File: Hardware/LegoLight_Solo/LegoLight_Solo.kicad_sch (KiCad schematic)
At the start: 37 parts, among them IC1 PAM2401SCADJ, J1 USB4105-GF-A, J2 103P012BB100, J3 103P012BB100, J4 Conn_01x02_Socket, J5 VEML7700-TT, J8 I2C, U1 MCP73831-2-OT, U2 KXTJ3-1057

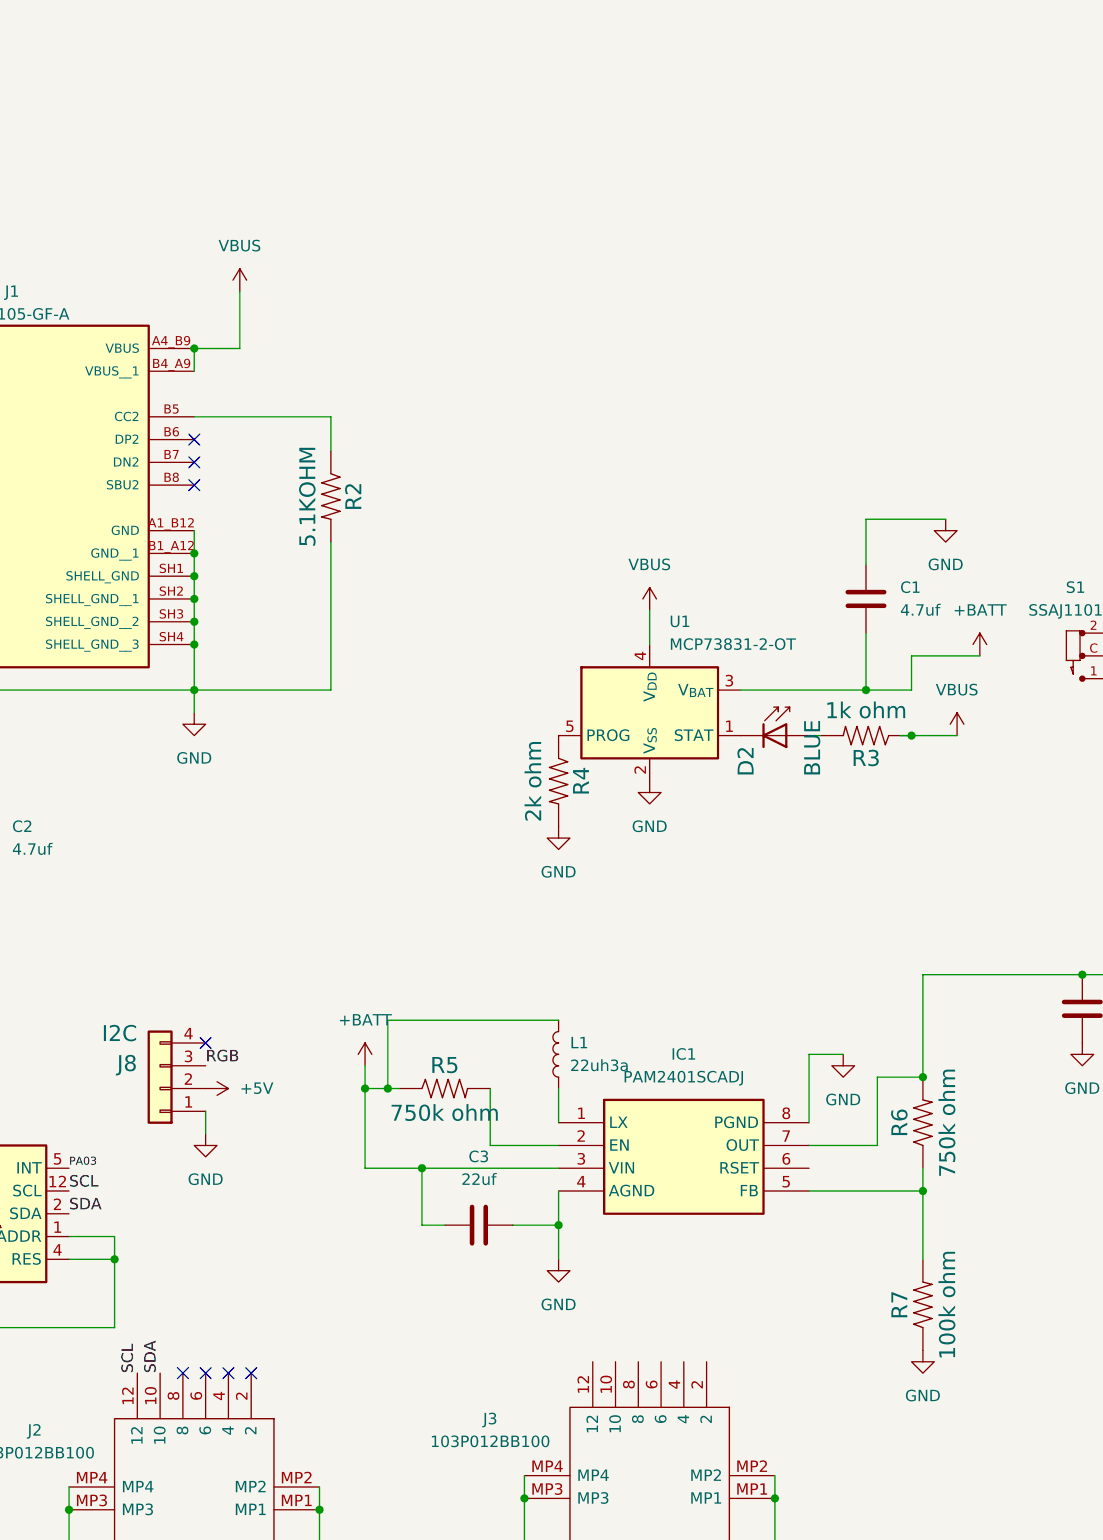
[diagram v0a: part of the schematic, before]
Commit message: add hq header to solo
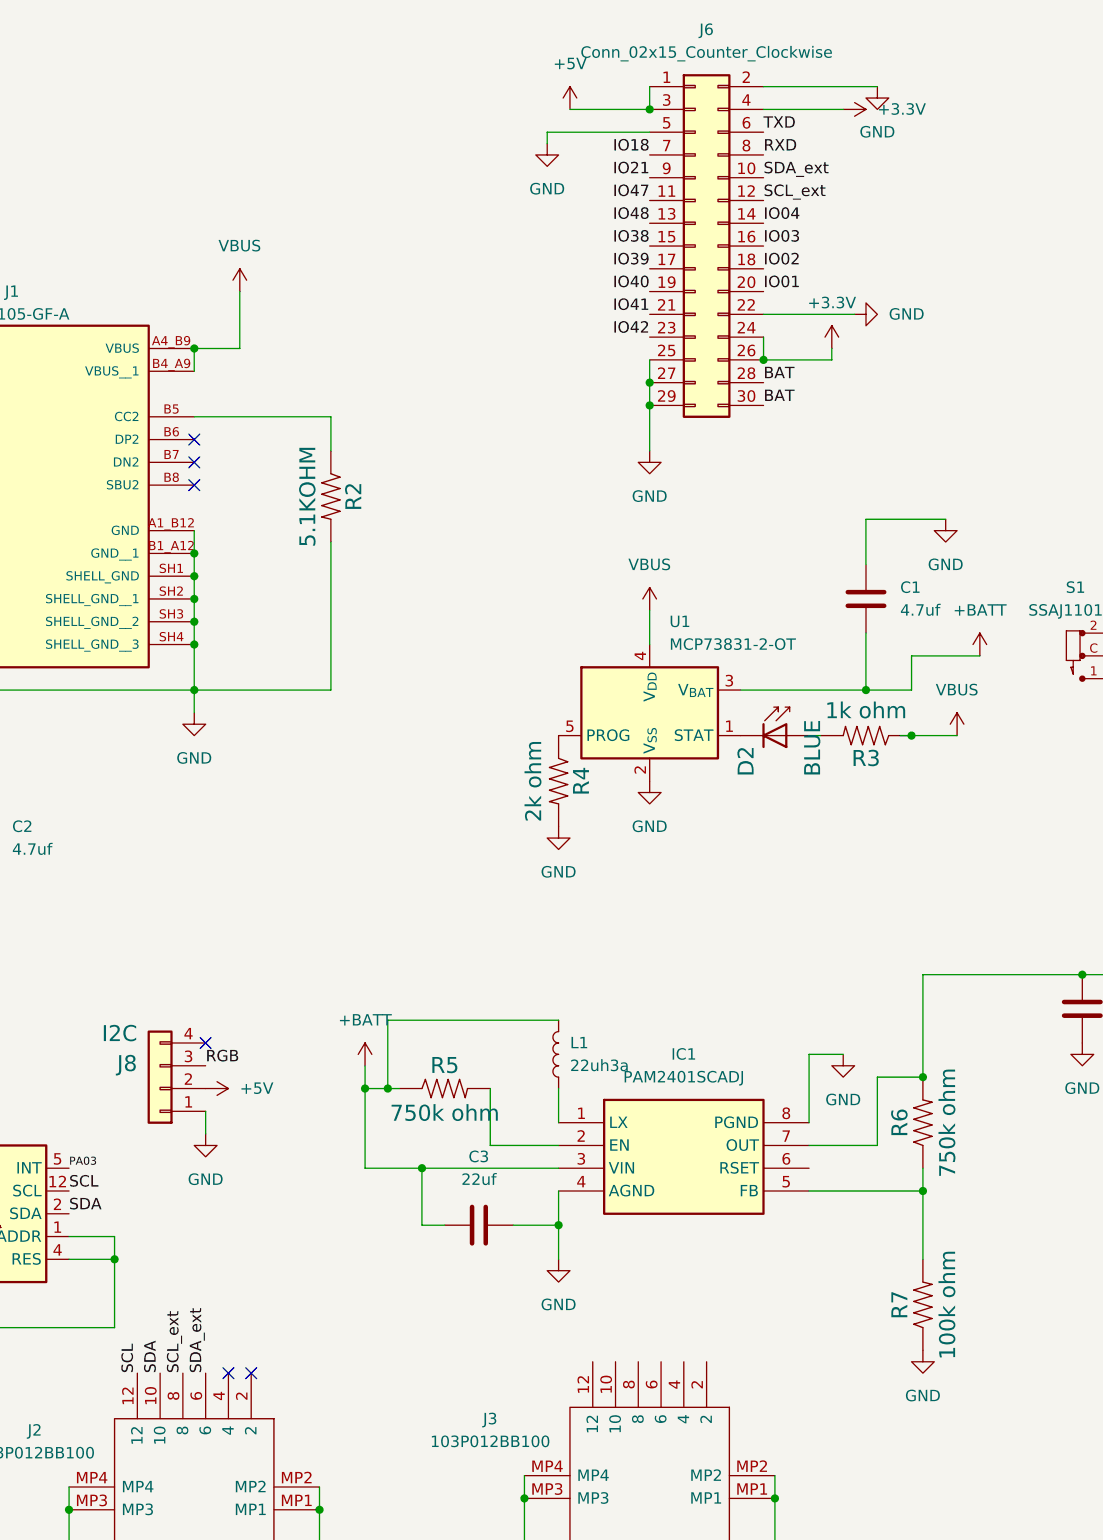
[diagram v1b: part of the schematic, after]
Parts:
- added J6: Conn_02x15_Counter_Clockwise, Connector_PinSocket_1.27mm:PinSocket_2x15_P1.27mm_Vertical, symbol Connector_Generic:Conn_02x15_Odd_Even
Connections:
- net +3.3V: now also J6.24 (Pin_24), J6.26 (Pin_26), J6.4 (Pin_4)
- net +5V: now also J6.1 (Pin_1), J6.3 (Pin_3)
- net GND: now also J6.2 (Pin_2), J6.22 (Pin_22), J6.25 (Pin_25), J6.27 (Pin_27), J6.29 (Pin_29), J6.5 (Pin_5)
- net SDA_ext: now reaches J2.6
- net SDA_ext: now also J6.10 (Pin_10)
- net SCL_ext: now reaches J2.8
- net SCL_ext: now also J6.12 (Pin_12)
- new net BAT: J6.28 (Pin_28), J6.30 (Pin_30)
- new net IO01: J6.20 (Pin_20)
- new net IO02: J6.18 (Pin_18)
- new net IO03: J6.16 (Pin_16)
- new net IO04: J6.14 (Pin_14)
- new net IO18: J6.7 (Pin_7)
- new net IO21: J6.9 (Pin_9)
- new net IO38: J6.15 (Pin_15)
- new net IO39: J6.17 (Pin_17)
- new net IO40: J6.19 (Pin_19)
- new net IO41: J6.21 (Pin_21)
- new net IO42: J6.23 (Pin_23)
- new net IO47: J6.11 (Pin_11)
- new net IO48: J6.13 (Pin_13)
- new net RXD: J6.8 (Pin_8)
- new net TXD: J6.6 (Pin_6)
- no-connect marks 11 -> 9

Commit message: final?
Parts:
- added BTN1: BTN, mouser:B3U-1000P, symbol Switch:SW_Push
- added J7: Conn_01x02_Socket, Connector_PinHeader_2.54mm:PinHeader_1x02_P2.54mm_Vertical, symbol Connector:Conn_01x02_Socket
- added R9: 10KOHM, Resistor_SMD:R_0805_2012Metric_Pad1.20x1.40mm_HandSolder, symbol SparkFun_Qwiic_Micro_SAMD21E-eagle-import:10KOHM-0402-1/16W-1%
- D10, D11, D12, D13, D6, D7, D8, D9: Mouser Part Number (none) -> 485-4492
- IC1: footprint SOP65P490X110-8N -> mouser:SOP65P490X110-8N
- J4: footprint Connector_JST:JST_SH_SM02B-SRSS-TB_1x02-1MP_P1.00mm_Horizontal -> Connector_JST:JST_PH_S2B-PH-SM4-TB_1x02-1MP_P2.00mm_Horizontal; Mouser Part Number (none) -> 485-1769
- L1: footprint Inductor_SMD:L_Vishay_IHLP-5050 -> Inductor_SMD:L_Taiyo-Yuden_MD-5050
- U2: footprint Package_LGA:Kionix_LGA-12_2x2mm_P0.5mm_LayoutBorder2x4y -> SnapEDA Library:KIONIX_KXTJ3-1057
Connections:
- net +3.3V: now also R9.2
- net GND: now also BTN1.1, J7.1 (Pin_1)
- net at J4.1 (Pin_1), S1.C: now also J7.2 (Pin_2)
- net PA07: now reaches J3.1
- net PA06: now reaches J3.3
- net PA05: now reaches J3.5
- net PA05: now also BTN1.2, R9.1
